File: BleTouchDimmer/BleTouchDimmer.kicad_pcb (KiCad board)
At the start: 2 copper layers, 113 x 56.1 mm, 65 parts, among them J1 Conn_01x03, J2 Conn_01x03, J3 JTAG, J4 Conn_01x06, J5 SLIDER1, J6 SLIDER2, P3 POWER, Q1 PDTC123J, Q2 PDTC123J, Q3 PDTC123J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

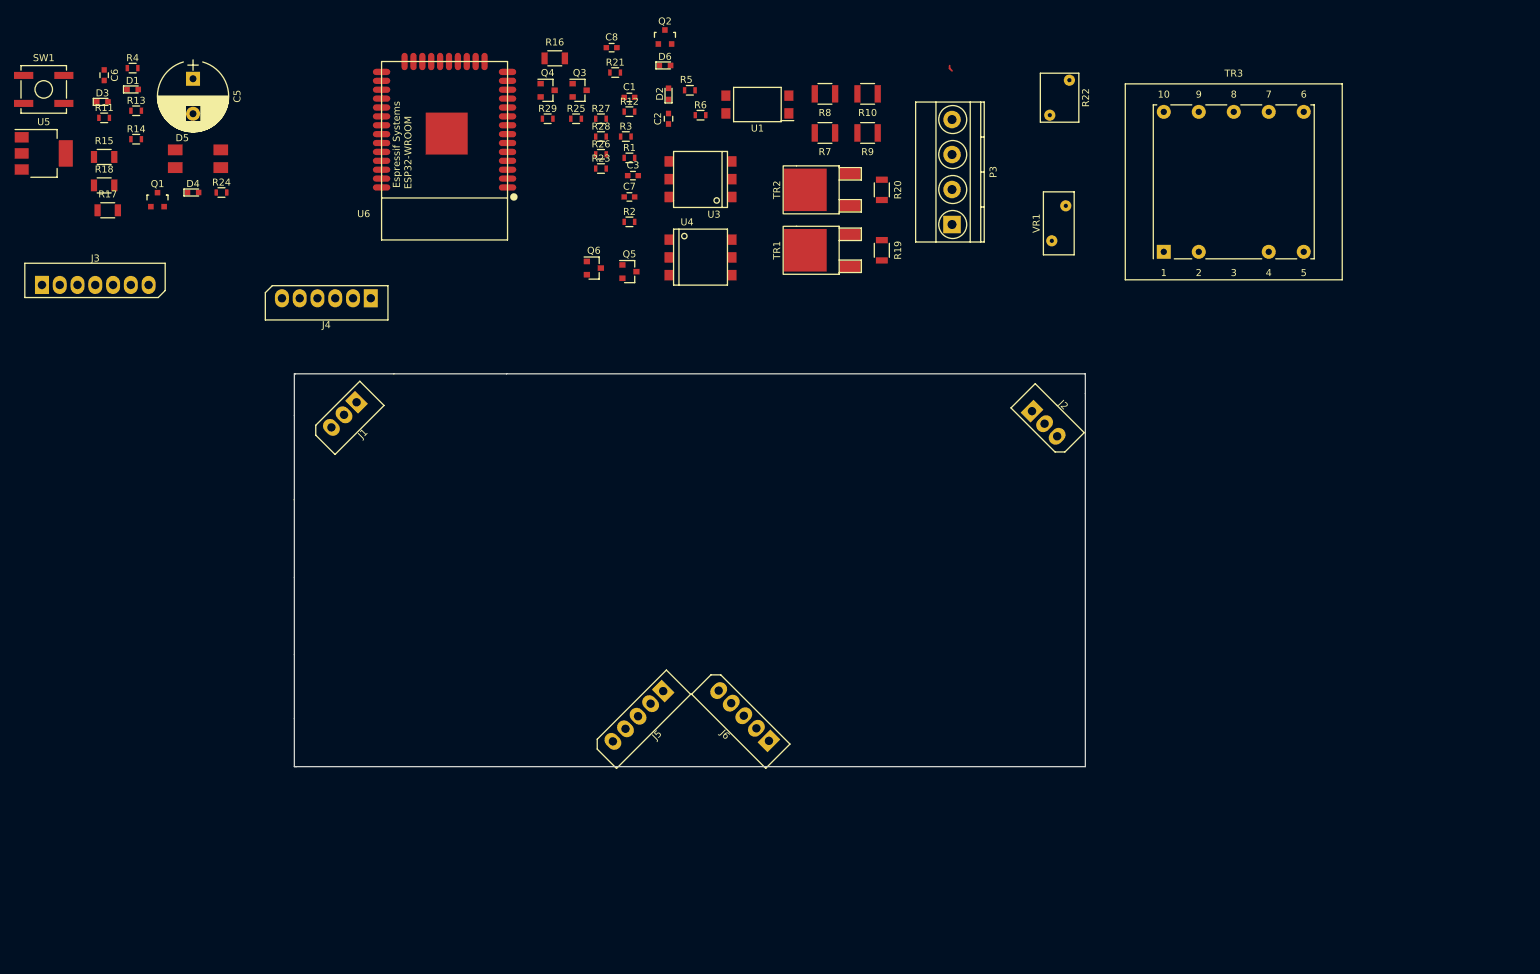
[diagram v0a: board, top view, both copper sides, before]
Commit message: Verified slider pcb position.
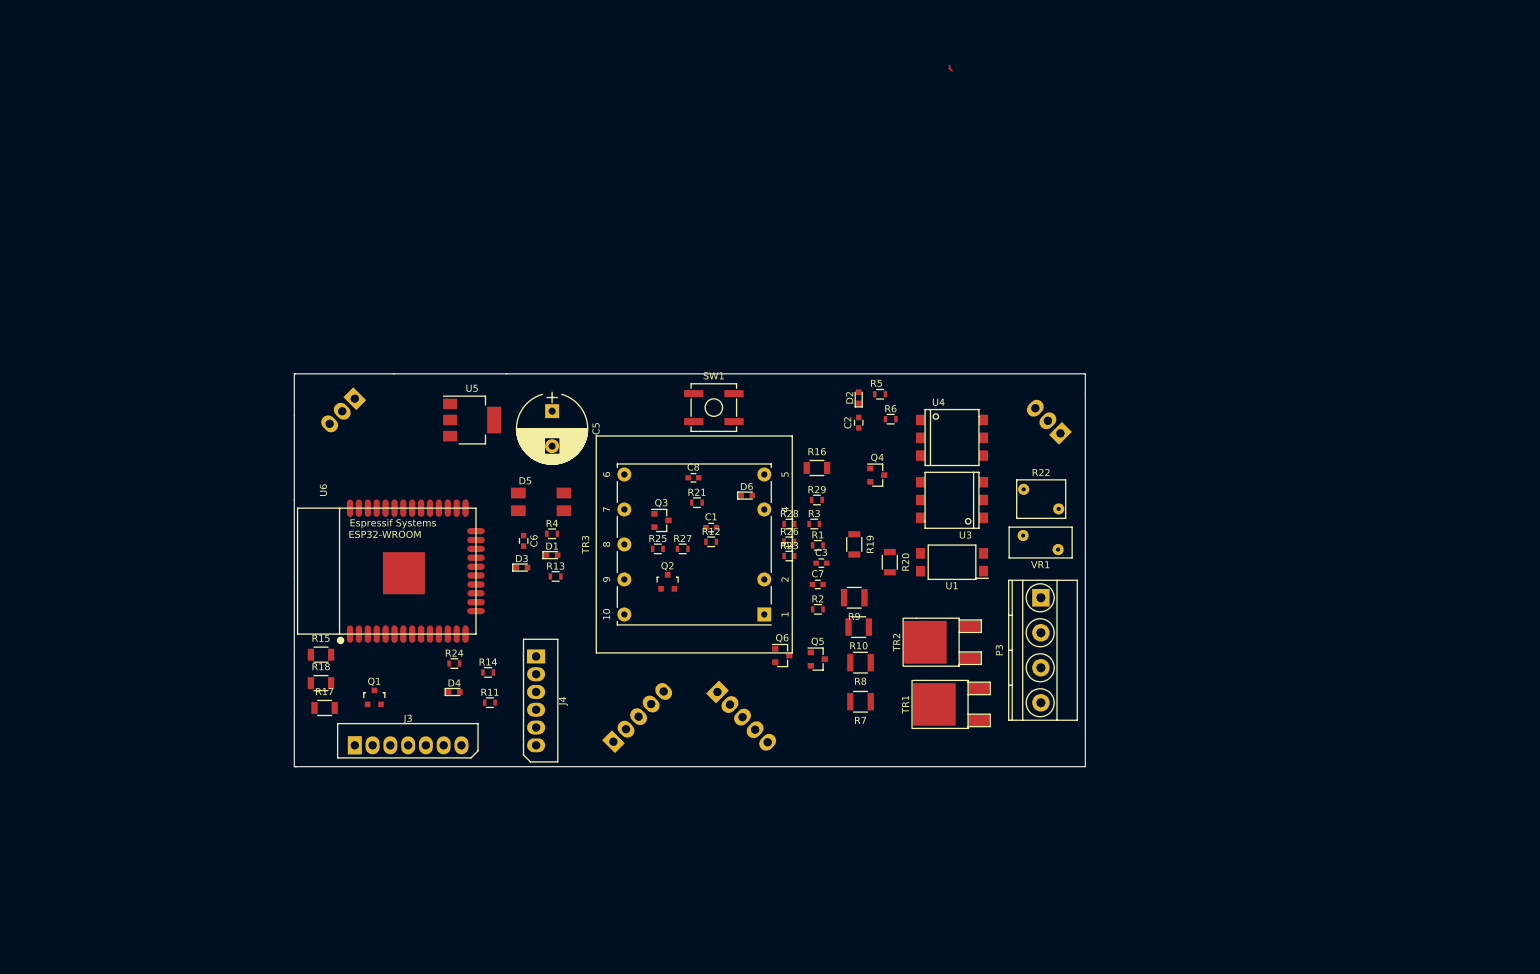
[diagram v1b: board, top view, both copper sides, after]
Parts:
- J1, J2, J5, J6: moved to B.Cu
- moved SW1 106.0 mm to (164.1, 68.1)
- moved R11 100.1 mm to (132.1, 110.2)
- moved TR3 92.9 mm to (161.3, 87.6), turned to 90 degrees
- moved R14 91.3 mm to (131.8, 105.9)
- moved C6 89.6 mm to (136.9, 87.1)
- moved D1 89.6 mm to (141.0, 89.2)
- moved D3 89.6 mm to (136.7, 90.9)
- moved R13 89.6 mm to (141.5, 92.2)
- moved R4 89.6 mm to (141.0, 86.1)
- moved R7 81.4 mm to (185.0, 110.1)
- moved R8 81.4 mm to (185.0, 104.5)
- moved D4 80.6 mm to (127.0, 108.7)
- moved J3 79.5 mm to (112.8, 116.3)
- moved Q2 77.9 mm to (157.5, 93.0)
- moved Q1 77.6 mm to (115.6, 109.5)
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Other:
- board text added: "A"
- board text added: "CP"
- board text added: "GND"
- board text added: "K"
- board text added: "SP1"
- board text added: "SP2"
- board text added: "SP3"

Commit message: Started routing triacs.
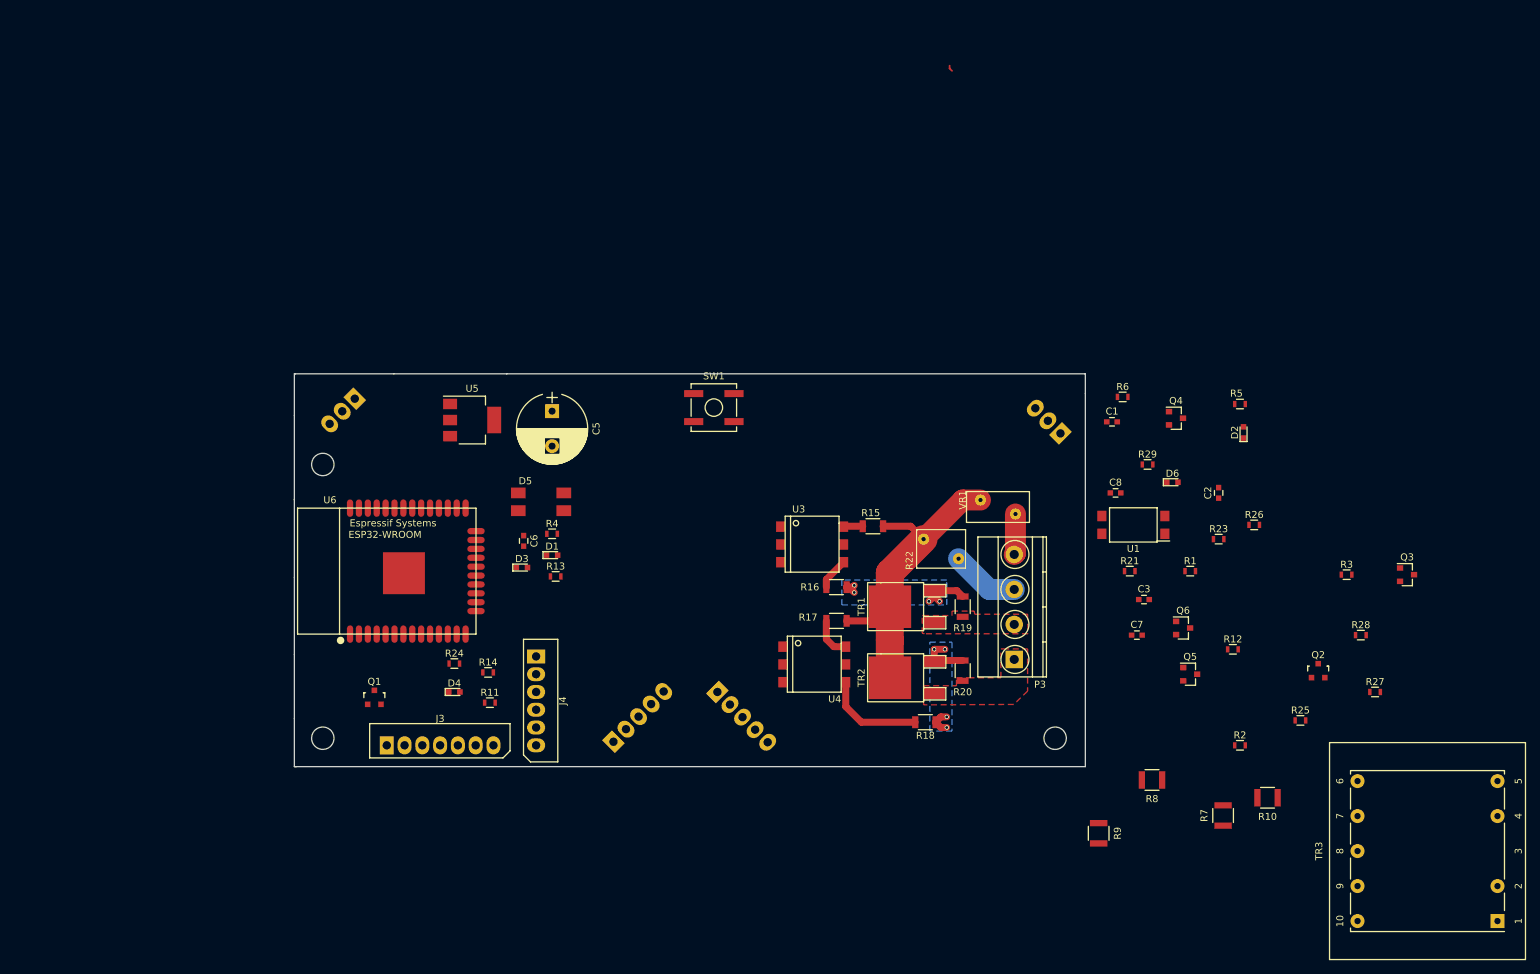
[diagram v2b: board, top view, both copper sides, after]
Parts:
- added REF**: MountingHole_3.2mm_M3, Mounting_Holes:MountingHole_3.2mm_M3, F.Cu at (108.2, 76.2)
- added REF**: MountingHole_3.2mm_M3, Mounting_Holes:MountingHole_3.2mm_M3, F.Cu at (108.2, 115.3)
- added REF**: MountingHole_3.2mm_M3, Mounting_Holes:MountingHole_3.2mm_M3, F.Cu at (212.9, 115.3)
- moved TR3 113.6 mm to (266.1, 131.4)
- moved Q3 106.8 mm to (263.1, 91.9)
- moved R27 101.0 mm to (258.6, 108.7)
- moved R25 95.0 mm to (247.9, 112.8)
- moved Q2 93.8 mm to (250.4, 105.7)
- moved R18 86.5 mm to (194.3, 113.0)
- moved R28 83.2 mm to (256.5, 100.6)
- moved R15 81.0 mm to (186.8, 85.0)
- moved R3 76.4 mm to (254.5, 91.9)
- moved R12 76.1 mm to (238.3, 102.6)
- moved R17 74.2 mm to (181.6, 98.6)
- moved R26 66.5 mm to (241.3, 84.8)
- moved R2 63.4 mm to (239.3, 116.3)
- moved R10 63.3 mm to (243.2, 123.8)
- moved R21 62.6 mm to (223.5, 91.4)
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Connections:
- P3 pad 1: /L_IN -> /TR2_L_OUT
- P3 pad 3: /TR2_L_OUT -> /L_IN
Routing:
- net /230_VAC_L: track 0.00 -> 45.8 mm
- net Net-(R18-Pad1): track 0.00 -> 14.3 mm
- net Net-(R18-Pad2): track 0.00 -> 11.3 mm, vias 0 -> 4
- net Net-(R16-Pad2): track 0.00 -> 9.93 mm, vias 0 -> 4
- net /L_IN: track 0.00 -> 9.77 mm
- net /N: track 0.00 -> 5.85 mm
- net Net-(R17-Pad1): track 0.00 -> 5.83 mm
- net Net-(R16-Pad1): track 0.00 -> 4.58 mm
- net Net-(R15-Pad1): track 0.00 -> 2.77 mm
- added copper zone on F.Cu, net /TR1_L_OUT
- added copper zone on F.Cu, net /TR2_L_OUT
- added copper zone on B.Cu, net Net-(R16-Pad2)
- added copper zone on B.Cu, net Net-(R18-Pad2)
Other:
- net class Default: clearance 0.2 -> 0.3; trace_width 0.25 -> 0.3
- rule trace_clearance: 0.2 -> 0.3

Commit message: Finished routing. Needs to be verified.
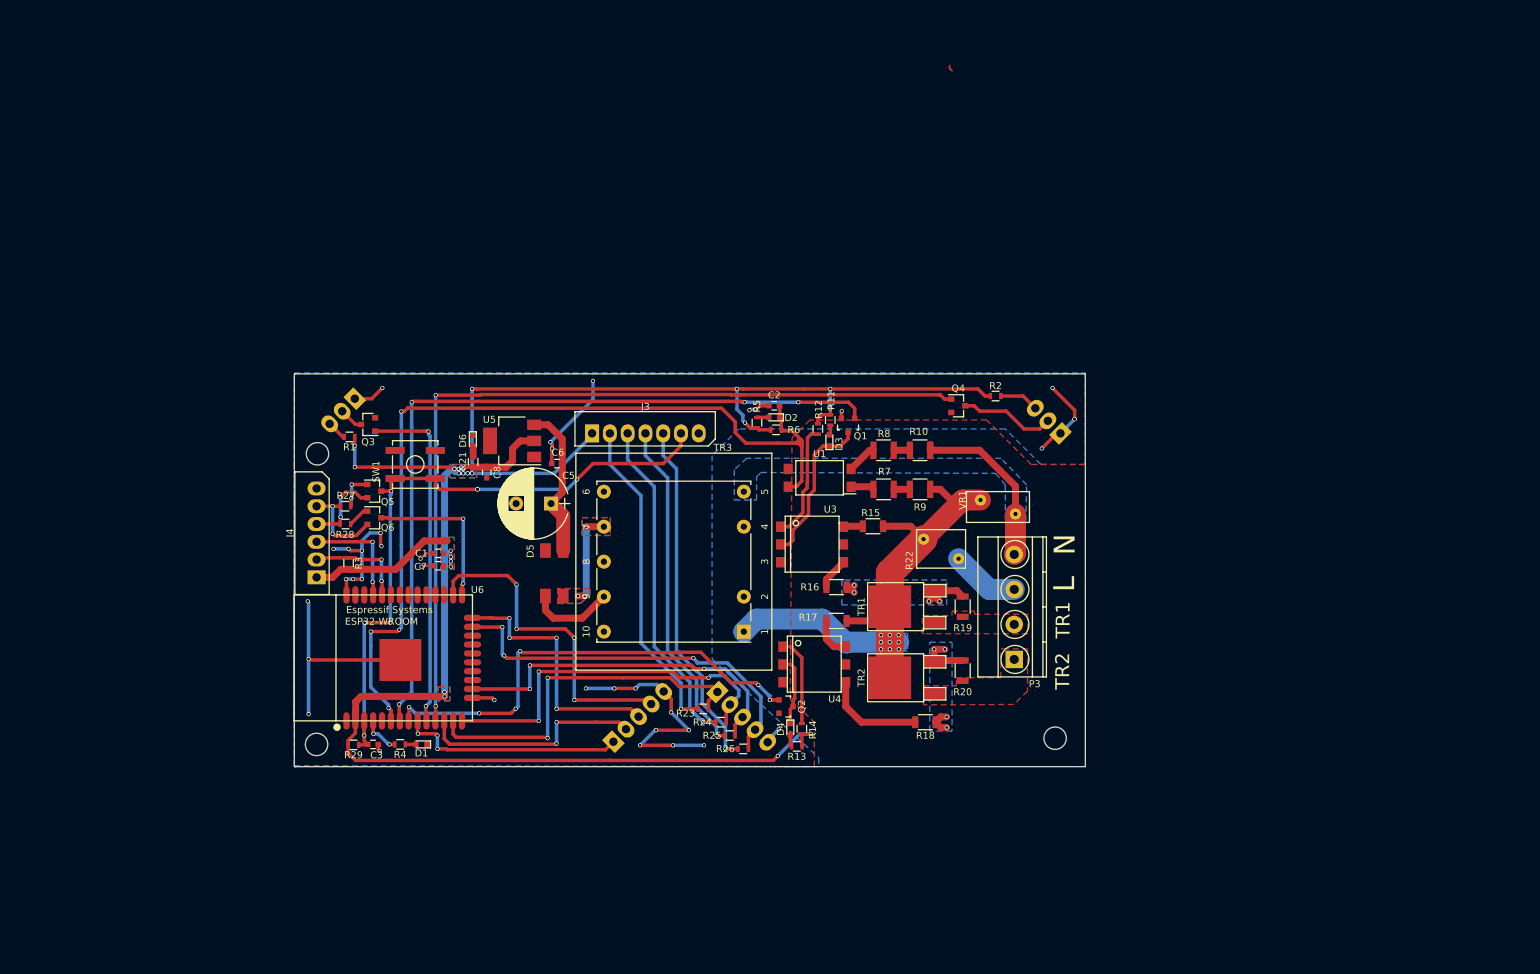
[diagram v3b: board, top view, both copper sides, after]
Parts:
- moved Q3 150.0 mm to (114.7, 70.5), turned to 180 degrees
- moved R27 149.5 mm to (111.4, 82.2), turned to 180 degrees
- moved R28 146.0 mm to (111.4, 84.7), turned to 180 degrees
- moved R3 142.6 mm to (111.9, 90.3), turned to 270 degrees
- moved R1 121.7 mm to (112.0, 72.3), turned to 180 degrees
- moved R29 120.3 mm to (112.6, 116.3), turned to 180 degrees
- moved Q5 119.5 mm to (115.6, 80.0)
- moved Q6 116.6 mm to (115.6, 83.8)
- moved TR3 115.4 mm to (158.4, 90.1)
- moved C3 112.1 mm to (115.4, 116.2), turned to 180 degrees
- moved C7 100.3 mm to (124.7, 90.7), turned to 180 degrees
- moved D6 100.1 mm to (129.6, 72.8), turned to 270 degrees
- moved C1 98.1 mm to (124.7, 88.9), turned to 180 degrees
- moved R21 95.1 mm to (129.7, 75.8), turned to 90 degrees
- moved C8 89.9 mm to (131.6, 77.3), turned to 270 degrees
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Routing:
- net +3V3: track 0.00 -> 309.6 mm, vias 0 -> 22
- net GND: track 0.00 -> 130.6 mm, vias 0 -> 36
- net /ZC_DETECT: track 0.00 -> 126.6 mm, vias 0 -> 4
- net /LED2: track 0.00 -> 120.6 mm, vias 0 -> 2
- net /TR1_CTRL: track 0.00 -> 111.5 mm, vias 0 -> 4
- net /RESET: track 0.00 -> 93.5 mm, vias 0 -> 7
- net /TR2_CTRL: track 0.00 -> 66.7 mm, vias 0 -> 6
- net /TOUCH3/MTDO: track 0.00 -> 55.9 mm, vias 0 -> 3
- net /TOUCH5/MTDI: track 0.00 -> 53.3 mm, vias 0 -> 3
- net /TOUCH6/MTMS: track 0.00 -> 52.3 mm, vias 0 -> 2
- net /TOUCH4/MTCK: track 0.00 -> 51.3 mm, vias 0 -> 3
- net Net-(J3-Pad5): track 0.00 -> 50.6 mm, vias 0 -> 1
- net /LED1: track 0.00 -> 49.4 mm, vias 0 -> 2
- net Net-(J3-Pad4): track 0.00 -> 49.4 mm, vias 0 -> 1
- net Net-(J3-Pad3): track 0.00 -> 47.5 mm, vias 0 -> 1
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- added copper zone on B.Cu, net +3V3
- added copper zone on F.Cu, net +3V3
- added copper zone on B.Cu, net /230_VAC_L
- added copper zone on B.Cu, net /N
- added copper zone on B.Cu, net GND
- added copper zone on F.Cu, net GND
- added copper zone on B.Cu, net Net-(D5-Pad4)
- added copper zone on F.Cu, net Net-(D5-Pad4)
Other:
- board text added: "L"
- board text added: "N"
- board text added: "TR1"
- board text added: "TR2"
